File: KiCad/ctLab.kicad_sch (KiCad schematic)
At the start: 0 parts

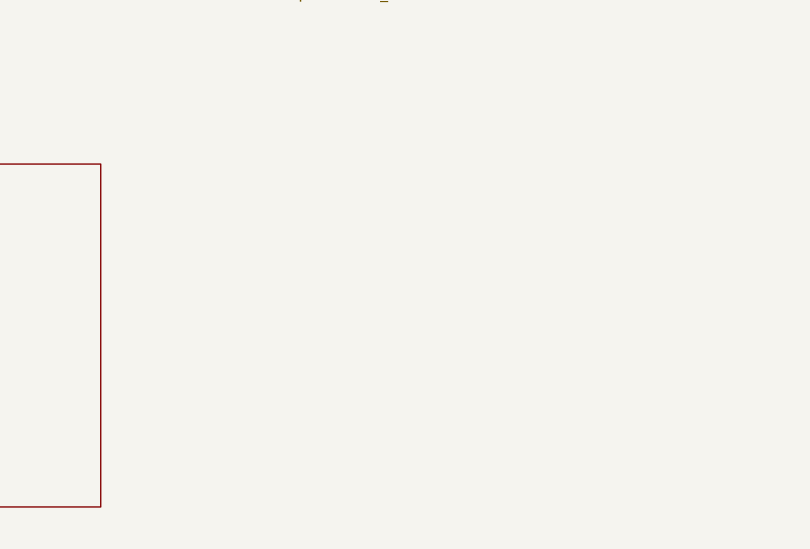
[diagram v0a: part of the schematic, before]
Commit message: adding IO8-32 schematics
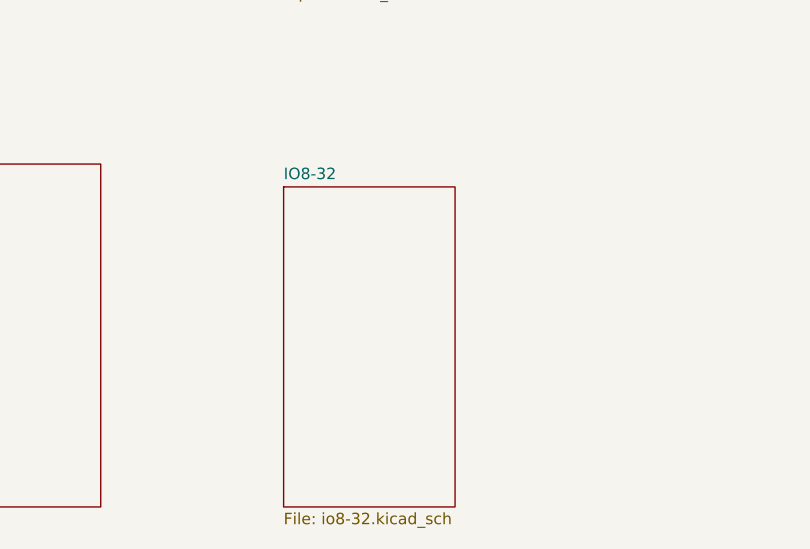
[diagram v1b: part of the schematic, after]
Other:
- added sheet IO8-32 (io8-32.kicad_sch)
- title: (none) -> c't Lab
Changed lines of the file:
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@@
 	(generator_version "10.0")
 	(paper "A3")
+	(title_block
+		(title "c't Lab")
+	)
 	(sheet
 		(at 274.32 31.75)
@@
 				)
 			)
+		)
+	)
+	(sheet
+		(at 276.86 96.52)
+		(size 19.05 35.56)
+		(exclude_from_sim no)
+		(in_bom yes)
+		(on_board yes)
+		(dnp no)
+		(fields_autoplaced yes)
+		(stroke
+			(width 0.1524)
+			(type solid)
+		)
+		(fill
+			(color 0 0 0 0)
+		)
+		(property "Sheetname" "IO8-32"
+			(at 276.86 95.8084 0)
+			(show_name no)
+			(do_not_autoplace no)
+			(effects
+				(font
+					(size 1.27 1.27)
+				)
+				(justify left bottom)
+			)
+		)
+		(property "Sheetfile" "io8-32.kicad_sch"
+			(at 276.86 132.6646 0)
+			(show_name no)
+			(do_not_autoplace no)
+			(effects
+				(font
+					(size 1.27 1.27)
+				)
+				(justify left top)
+			)
+		)
+		(instances
+			(project "ctLab"
+				(path "/207e0f0e-27e8-440d-b34e-edbac4dab547"
+					(page "9")
+				)
+			)

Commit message: starting DIV
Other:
- added sheet DIV (Digital Voltmeter) (div.kicad_sch)
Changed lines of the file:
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@@
+		)
+	)
+	(sheet
+		(at 312.42 97.79)
+		(size 52.07 39.37)
+		(exclude_from_sim no)
+		(in_bom yes)
+		(on_board yes)
+		(dnp no)
+		(fields_autoplaced yes)
+		(stroke
+			(width 0.1524)
+			(type solid)
+		)
+		(fill
+			(color 0 0 0 0)
+		)
+		(property "Sheetname" "DIV (Digital Voltmeter)"
+			(at 312.42 97.0784 0)
+			(show_name no)
+			(do_not_autoplace no)
+			(effects
+				(font
+					(size 1.27 1.27)
+				)
+				(justify left bottom)
+			)
+		)
+		(property "Sheetfile" "div.kicad_sch"
+			(at 312.42 137.7446 0)
+			(show_name no)
+			(do_not_autoplace no)
+			(effects
+				(font
+					(size 1.27 1.27)
+				)
+				(justify left top)
+			)
+		)
+		(instances
+			(project "ctLab"
+				(path "/207e0f0e-27e8-440d-b34e-edbac4dab547"
+					(page "10")
+				)
+			)
 		)
 	)

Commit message: cont. div
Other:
- added sheet ADC192 (adc192.kicad_sch)
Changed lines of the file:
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@@
+	)
+	(sheet
+		(at 35.56 149.86)
+		(size 60.96 39.37)
+		(exclude_from_sim no)
+		(in_bom yes)
+		(on_board yes)
+		(dnp no)
+		(fields_autoplaced yes)
+		(stroke
+			(width 0.1524)
+			(type solid)
+		)
+		(fill
+			(color 0 0 0 0)
+		)
+		(property "Sheetname" "ADC192"
+			(at 35.56 149.1484 0)
+			(show_name no)
+			(do_not_autoplace no)
+			(effects
+				(font
+					(size 1.27 1.27)
+				)
+				(justify left bottom)
+			)
+		)
+		(property "Sheetfile" "adc192.kicad_sch"
+			(at 35.56 189.8146 0)
+			(show_name no)
+			(do_not_autoplace no)
+			(effects
+				(font
+					(size 1.27 1.27)
+				)
+				(justify left top)
+			)
+		)
+		(instances
+			(project "ctLab"
+				(path "/207e0f0e-27e8-440d-b34e-edbac4dab547"
+					(page "11")
+				)
+			)
+		)
 	)
 	(sheet
